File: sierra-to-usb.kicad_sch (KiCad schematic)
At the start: 0 parts

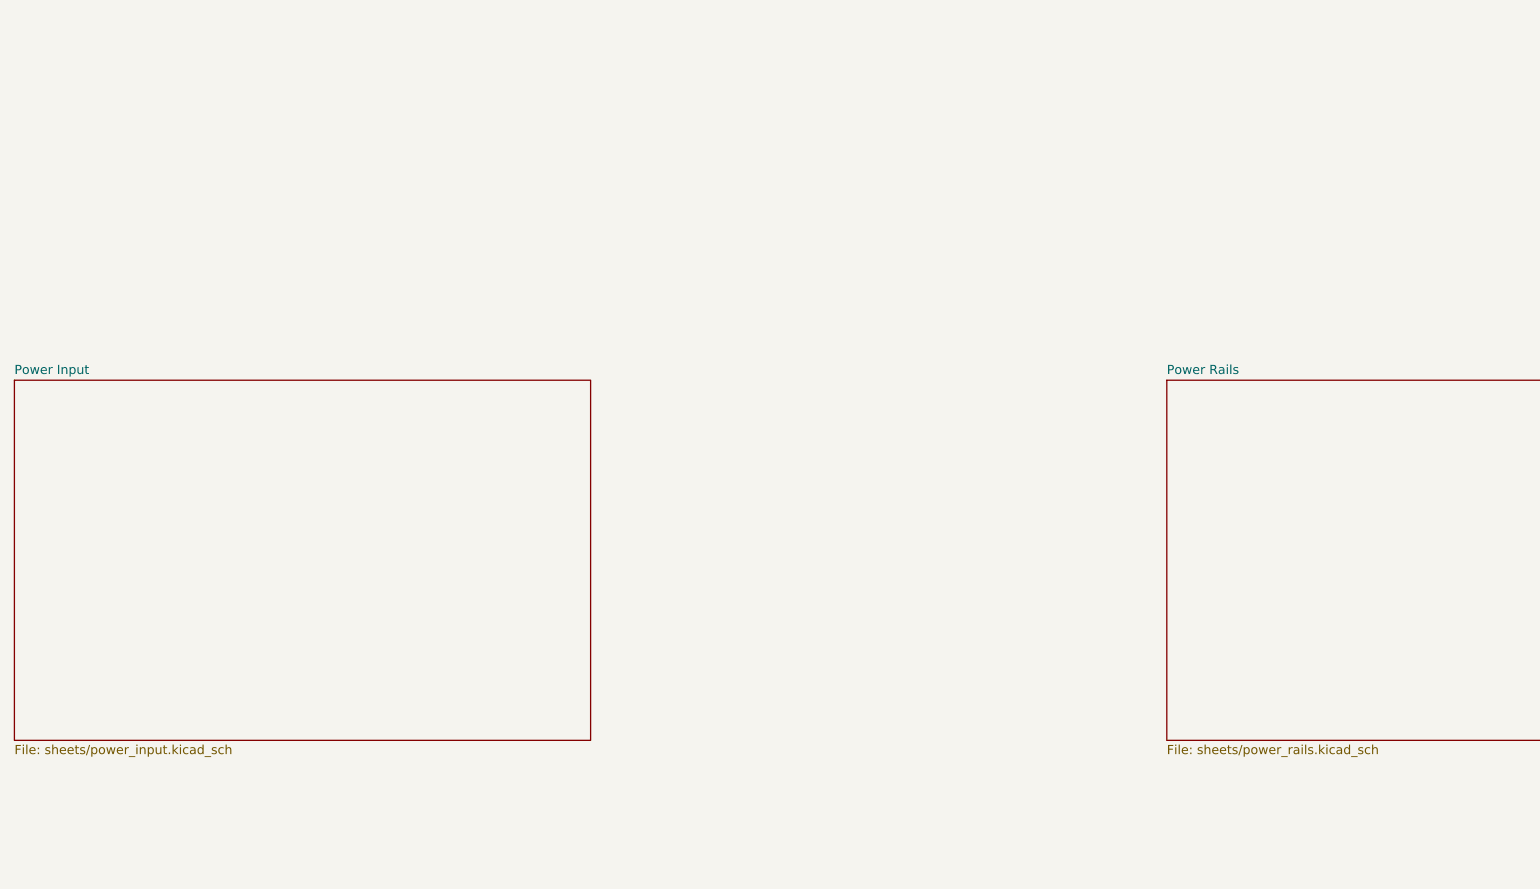
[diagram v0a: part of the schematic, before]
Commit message: sch: finish USB-C symbol-swap rework, fix grid-snap shorts + BR pinout
User rework completed: J1/J3 (Connector:USB_C_Receptacle) rewired to their
HEAD net maps (J1 nudged on-grid), J2 PD data lines (R98/R83 -> CH224K
DP/DM) locked into netchecks, MDB10S bridges relabeled so +/- feed
POE_VDD54/POE_VSS and ~ pins take POE_VA/VB pairs, C58/C59 moved off
U1's CC2/TX2P/RX2P pins (grid-snap had stacked their pin ends), R79
moved off R78.2's node (same failure mode), CH224K_VDD flag-farm label
renamed, USB2_MOD_D+/- reverted to canonical USB2_MOD_DP/DM, stale
debris labels and orphan GND symbols deleted.

check_nets: all pass. ERC: 0. Netlist diff vs HEAD = intentional only.

Co-Authored-By: Claude Fable 5 <noreply@anthropic.com>
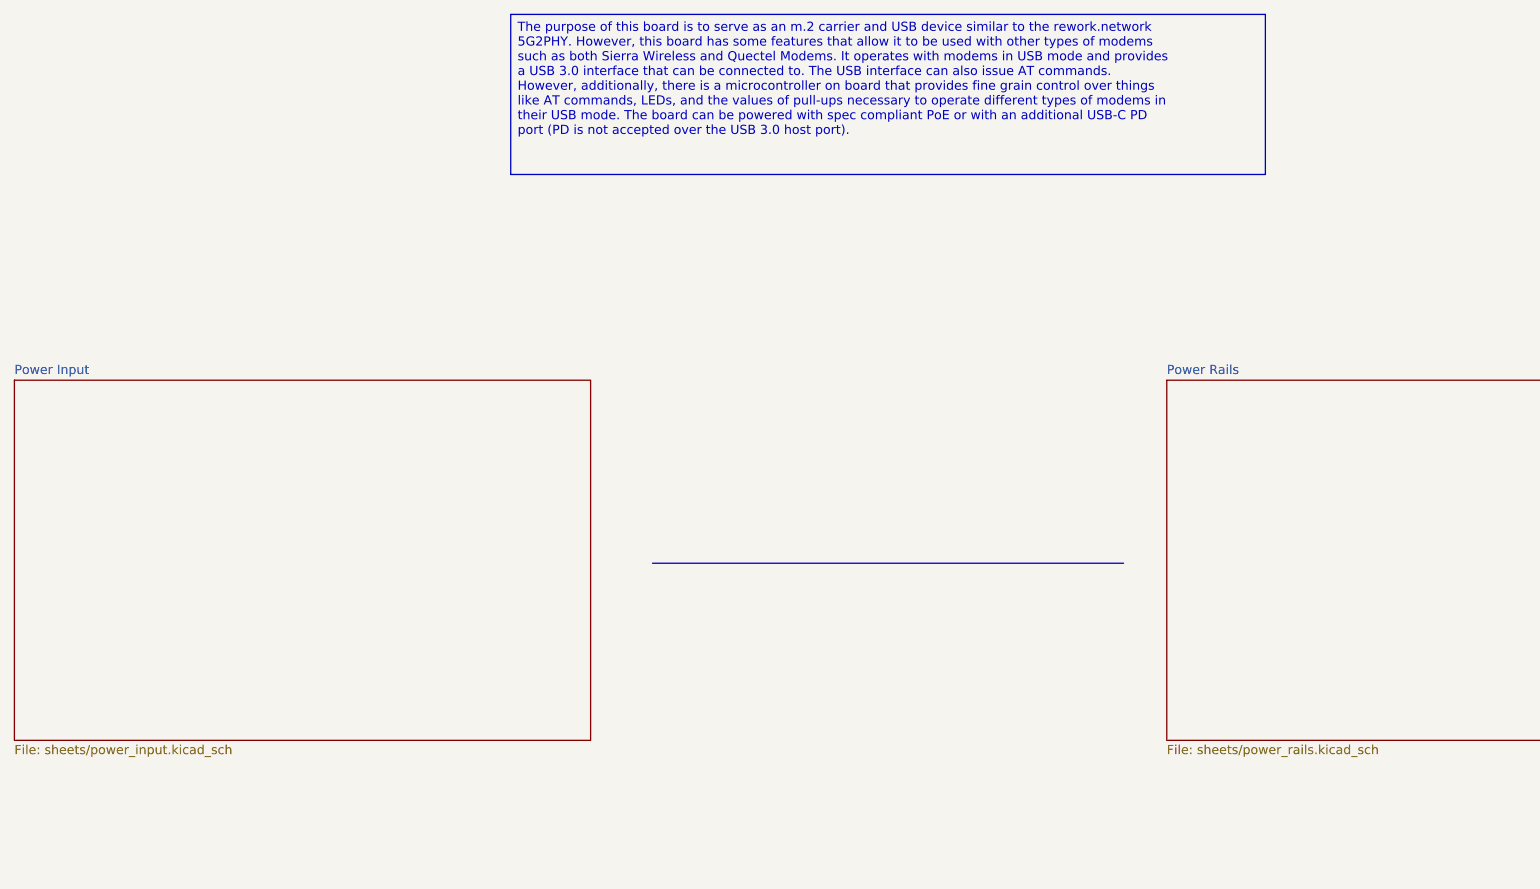
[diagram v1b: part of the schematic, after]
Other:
- company: (none) -> Alex Gompper
- title: (none) -> M.2 5G Modem Carrier
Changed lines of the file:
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@@
 	(generator_version "10.0")
 	(paper "A0")
+	(title_block
+		(title "M.2 5G Modem Carrier")
+		(date "2026-07-19")
+		(rev "A")
+		(company "Alex Gompper")
+	)
+	(text_box "The purpose of this board is to serve as an m.2 carrier and USB device similar to the rework.network 5G2PHY. However, this board has some features that allow it to be used with other types of modems such as both Sierra Wireless and Quectel Modems. It operates with modems in USB mode and provides a USB 3.0 interface that can be connected to. The USB interface can also issue AT commands. However, additionally, there is a microcontroller on board that provides fine grain control over things like AT commands, LEDs, and the values of pull-ups necessary to operate different types of modems in their USB mode. The board can be powered with spec compliant PoE or with an additional USB-C PD port (PD is not accepted over the USB 3.0 host port). "
+		(exclude_from_sim no)
+		(at 168.91 29.21 0)
+		(size 104.775 22.225)
+		(margins 0.9525 0.9525 0.9525 0.9525)
+		(stroke
+			(width 0)
+			(type solid)
+		)
+		(fill
+			(type none)
+		)
+		(effects
+			(font
+				(size 1.27 1.27)
+			)
+			(justify left top)
+		)
+	)
+	(polyline
+		(pts
+			(xy 188.595 105.41) (xy 254 105.41)
+		)
+		(stroke
+			(width 0)
+			(type default)
+		)
+	)
 	(sheet
 		(at 420 190)
@@
 		)
 		(property "Sheetname" "Power Input"
-			(at 100 79.29 0)
+			(at 100 79.2884 0)
 			(show_name no)
 			(do_not_autoplace no)
@@
 		)
 		(property "Sheetfile" "sheets/power_input.kicad_sch"
-			(at 100 130.58 0)
-			(show_name no)
-			(do_not_autoplace no)
+			(at 100 130.5846 0)
+			(show_name no)
+			(do_not_autoplace no)

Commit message: sch: lay out root page as the system block diagram
Reposition the 9 sheet blocks on the root page into architecture
topology -- power band across the top, edge-I/O column feeding a tall
M.2 block, RF and MCU on the right -- and add 12 text annotations naming
the inter-block buses, the rails out of Power Rails, and what the MCU
drives.

Cosmetic only: no component moved, no sheet renamed, no net renamed.
Child sheets and the PCB are untouched. check_nets passes, and
check_netclasses reports 51/51 POE_PRI nets, so the 2.5mm moat is
intact. ERC 0 errors.

Known gap: KiCad stores a sheet's Sheetname/Sheetfile label positions as
absolute coordinates, and neither Konnect nor the kicad MCP server can
move them (set_sheet_property refuses built-ins; autoplace_schematic_fields
only handles component Reference/Value). Those labels are still at their
old grid positions and need one pass of field autoplacement in eeschema.

Co-Authored-By: Claude Opus 5 <noreply@anthropic.com>
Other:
- note added: "+12 V"
- note added: "ANT0-3, GNSS --> MHF4 jumpers"
- note added: "All inter-sheet connectivity is by global label - these blocks show topology, not sheet pins. Power rails reach every sheet the same way."
- note added: "Control plane"
- note added: "PCIe x1 <--> CN1 41/43 (mod TX), 47/49 (mod RX), 53/55 REFCLK"
- note added: "Power"
- note added: "Signal path - edge I/O to module"
- note added: "UIM1 --> CN1 30-36 UIM2 (mux: nano-SIM 2 / eSIM) --> CN1 40-48"
- note added: "USB2 D+/- --> CN1 7/9 (mux A = data port, B = RP2040 PIO-USB host)"
- note added: "USB3 SS --> CN1 29/31 (module TX), 35/37 (module RX)"
- note added: "drives: straps CN1 6/8/20/22/67 | USB2 mux select | SIM select | RTL8125 reset | I2C telemetry"
- note added: "rails out: +3V3 -> +3V3_MOD (M.2 VCC) | +1V8 (straps) | +3V3_ETH -> +0V95 (RTL core) | +3V3_MCU | +3V3_MUX"
